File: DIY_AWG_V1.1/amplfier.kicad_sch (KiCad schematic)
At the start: 21 parts, among them IC3 THS3091DDAR, IC4 LMH6505MAX, J3 Conn_Coaxial

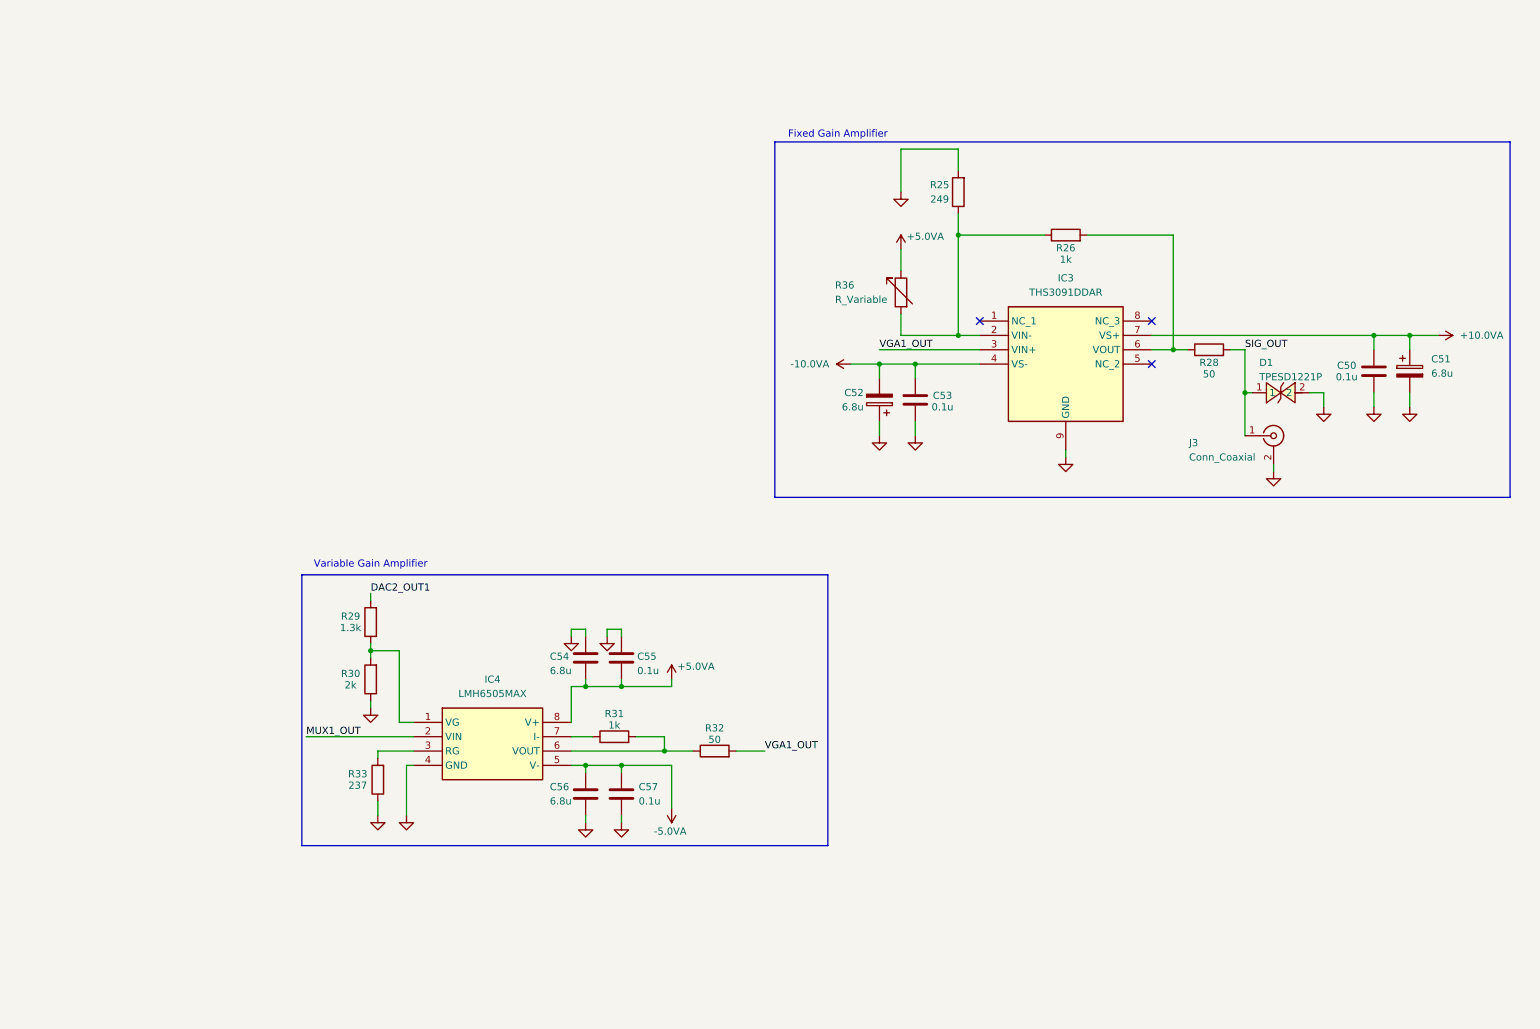
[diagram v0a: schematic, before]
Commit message: Updated the schematic AD9834_DDS
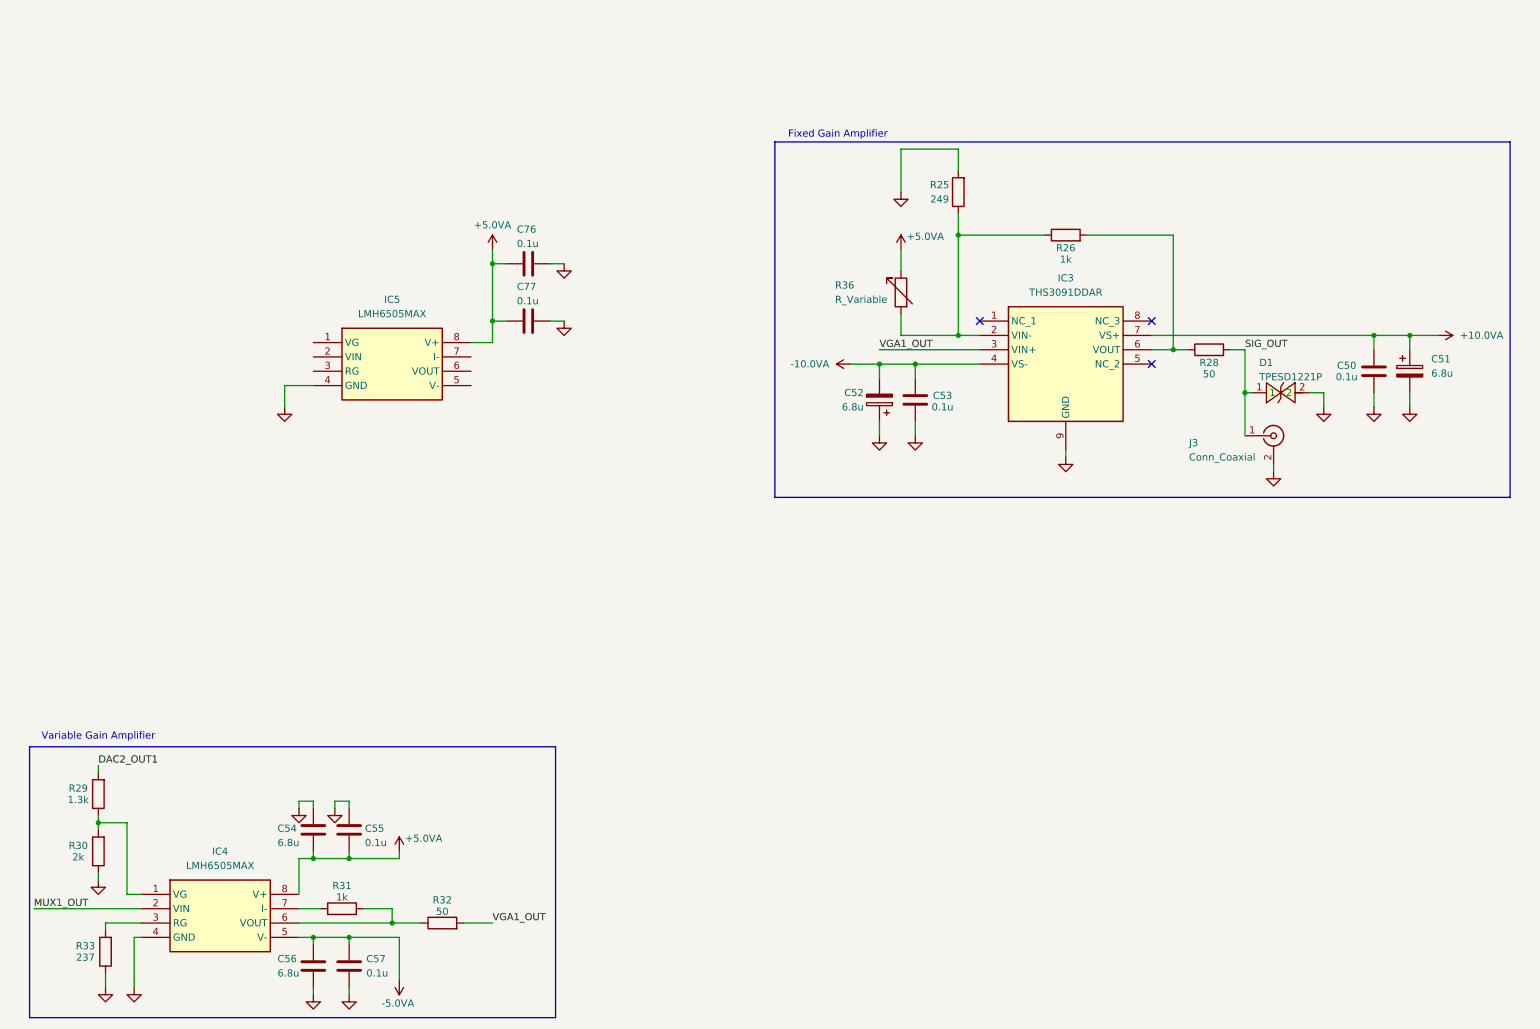
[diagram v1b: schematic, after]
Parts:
- added C76, C77: 0.1u, symbol Device:C
- added IC5: LMH6505MAX, SOIC127P600X175-8N, symbol LMH6505MAX:LMH6505MAX
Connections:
- net +5.0VA: now also C76.1, C77.1, IC5.8 (V+)
- net GND: now also C76.2, C77.2, IC5.4 (GND)
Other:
- moved on the sheet: C54, C55, C56, C57, IC4, R29, R30, R31, R32, R33

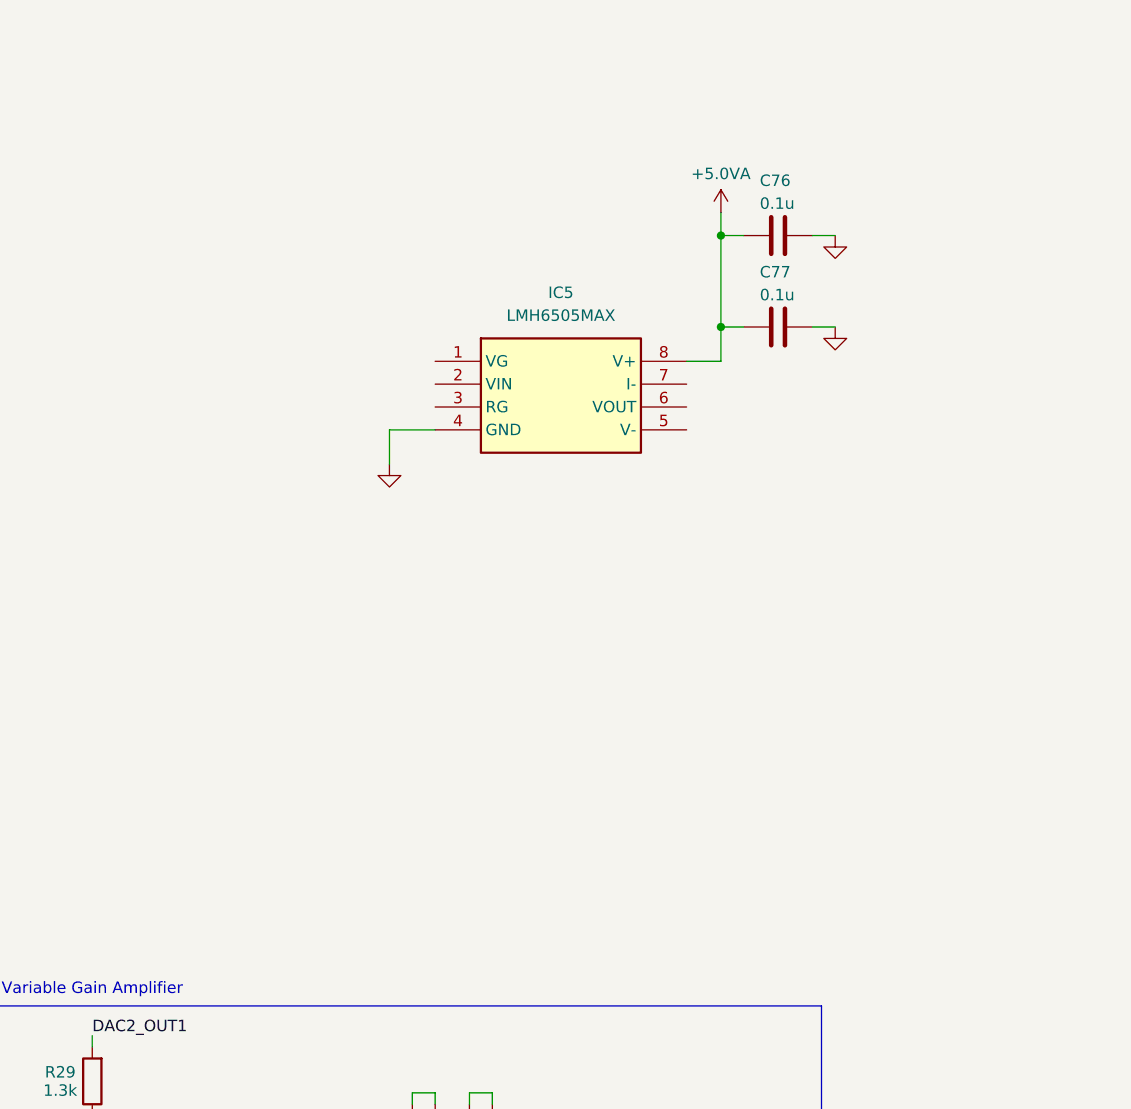
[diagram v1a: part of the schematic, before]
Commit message: Updated schematic AD9834_DDS, amplifier
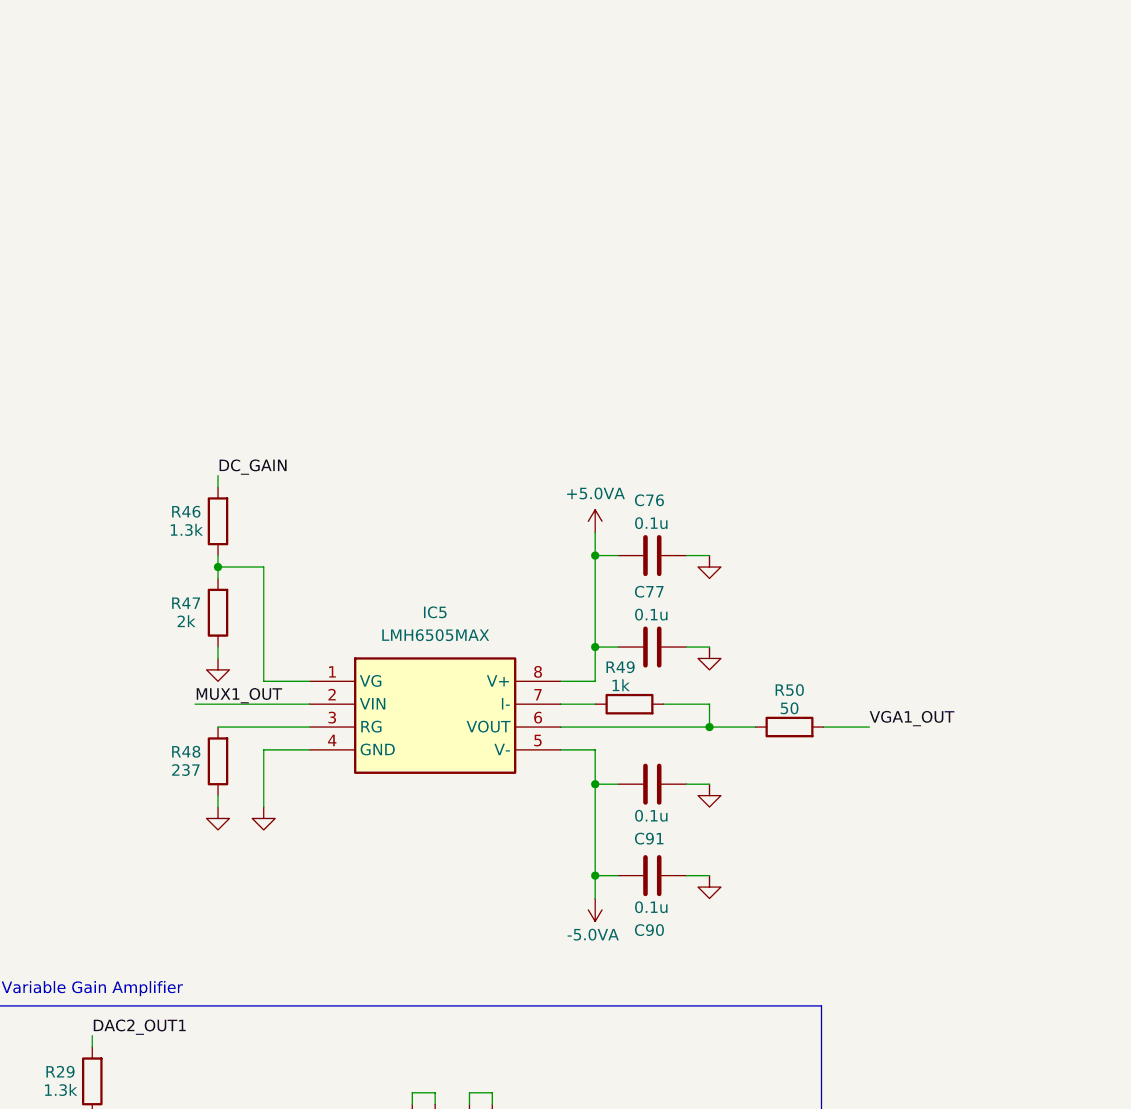
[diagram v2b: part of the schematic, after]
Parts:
- added C90, C91: 0.1u, symbol Device:C
- added R46: 1.3k, symbol Device:R
- added R47: 2k, symbol Device:R
- added R48: 237, symbol Device:R
- added R49: 1k, symbol Device:R
- added R50: 50, symbol Device:R
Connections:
- net -5.0VA: now also IC5.5 (V-), C90.1, C91.1
- net GND: now also C90.2, C91.2, R47.1, R48.1
- net MUX1_OUT: now also IC5.2 (VIN)
- net VGA1_OUT: now also R50.2
- net at IC5.1 (VG): now also R46.1, R47.2
- net at IC5.3 (RG): now also R48.2
- net at IC5.6 (VOUT): now also R49.2, R50.1
- net at IC5.7 (I-): now also R49.1
- new net DC_GAIN: R46.2
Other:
- moved on the sheet: C76, C77, IC5

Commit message: Updated AD9834_DDS and amplifier schematic
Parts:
- C77, C90: value 0.1u -> 6.8u
- R50: value 50 -> 0
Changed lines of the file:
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@@
 			)
 		)
-		(property "Value" "0.1u"
+		(property "Value" "6.8u"
 			(at 89.408 100.584 90)
 			(show_name no)
@@
 			)
 		)
-		(property "Value" "50"
+		(property "Value" "0"
 			(at 106.68 110.998 90)
 			(show_name no)
@@
 			)
 		)
-		(property "Value" "0.1u"
+		(property "Value" "6.8u"
 			(at 89.408 133.096 90)
 			(show_name no)

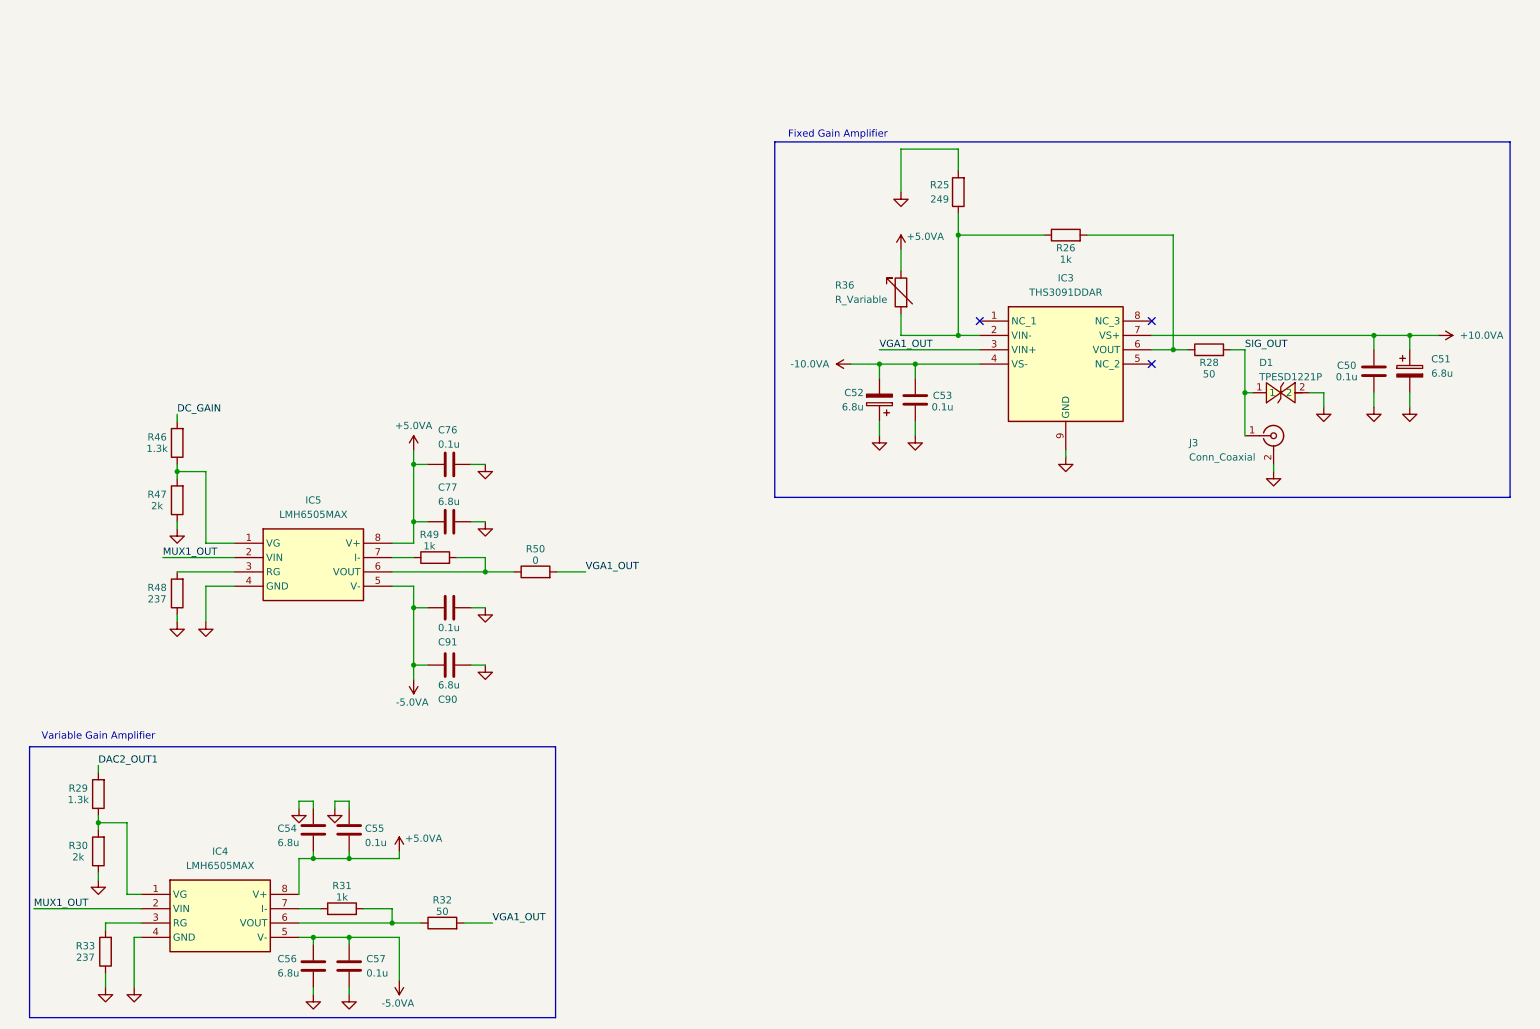
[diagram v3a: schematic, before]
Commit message: Updated AD9834_DDS, STM32_MCU, amplifier schematic
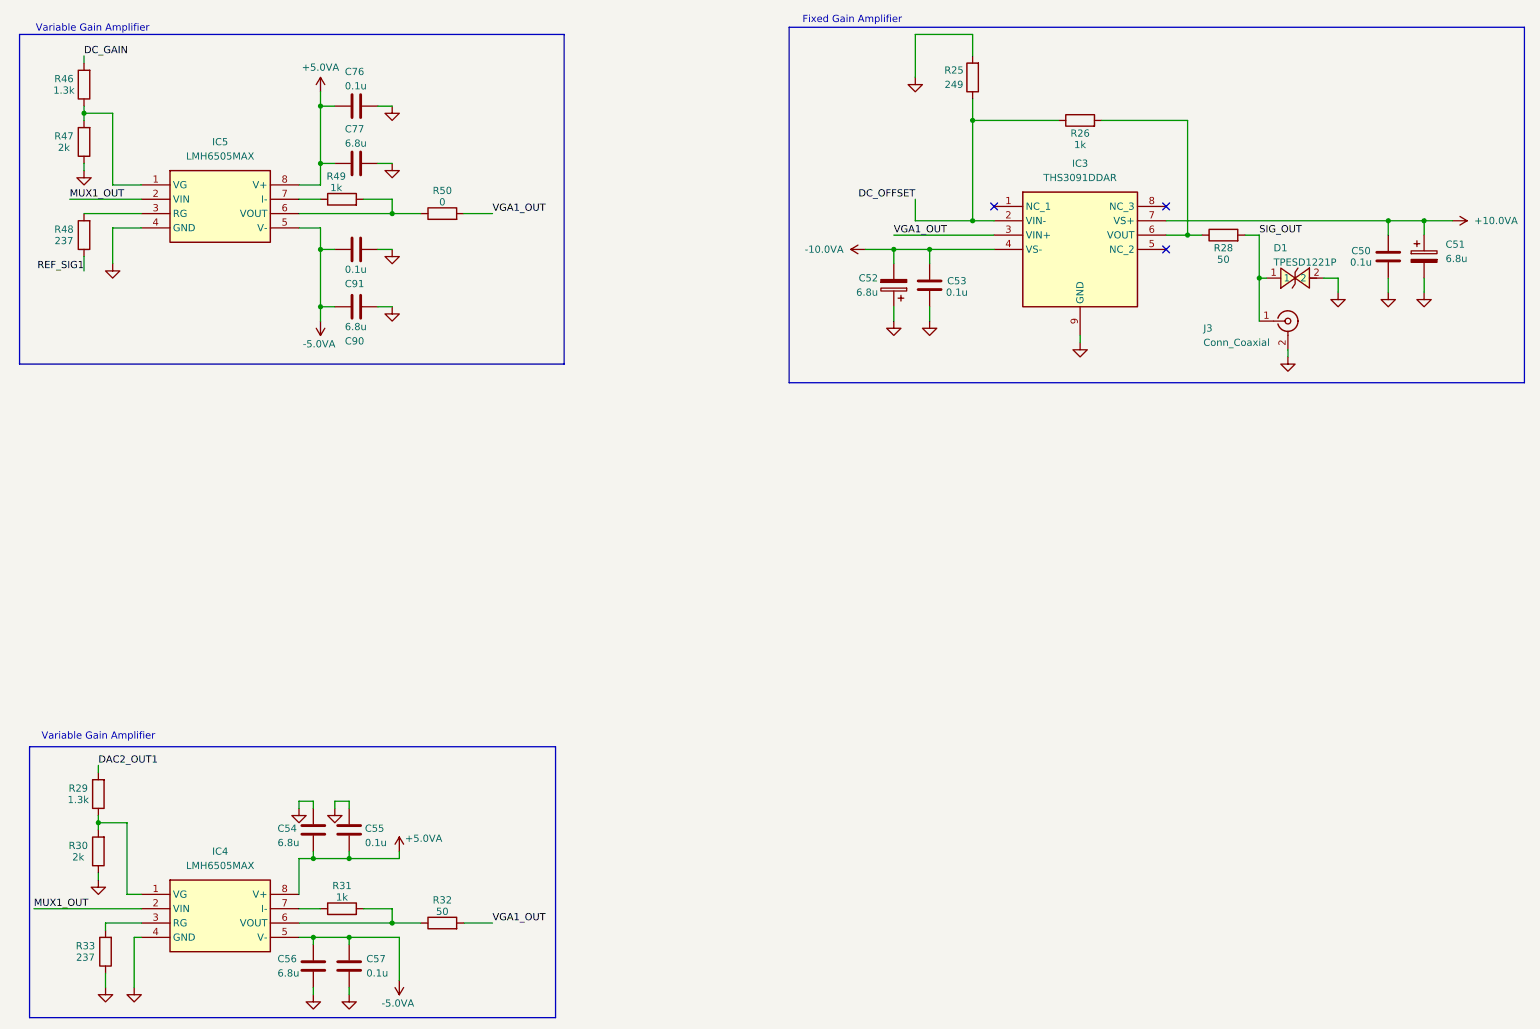
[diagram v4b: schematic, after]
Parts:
- removed R36: R_Variable, symbol Device:R_Variable
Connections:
- net GND: no longer R48.1
- net DC_OFFSET: now reaches IC3.2 (VIN-), R25.1, R26.1
- new net REF_SIG1: R48.1
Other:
- moved on the sheet: C50, C51, C52, C53, C76, C77, C90, C91, D1, IC3, IC5, J3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

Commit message: Updated AD9834_DDS, amplifier schematic
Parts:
- removed C54, C56: 6.8u, symbol Device:C
- removed C55, C57: 0.1u, symbol Device:C
- removed IC4: LMH6505MAX, SOIC127P600X175-8N, symbol LMH6505MAX:LMH6505MAX
- removed R29: 1.3k, symbol Device:R
- removed R30: 2k, symbol Device:R
- removed R31: 1k, symbol Device:R
- removed R32: 50, symbol Device:R
- removed R33: 237, symbol Device:R
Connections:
- net DC_OFFSET: now also R25.2; no longer IC3.2 (VIN-), R25.1, R26.1
- net GND: no longer R25.2
- new net: IC3.2 (VIN-), R25.1, R26.1
